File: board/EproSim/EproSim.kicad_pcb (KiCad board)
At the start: 2 copper layers, 85 parts, among them J1 AVR-ISP-6, J2 RS232, J3 Power IN, J4 EXT_ADDR, J5 EXT_D, J6 External Reset, Q1 2N3904, SW1 SW_Push, SW2 Power, U1 ATmega8A-PU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

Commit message: Begin organizing ROsiM board
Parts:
- moved J5 194.8 mm to (114.0, 163.7)
- moved H1 163.7 mm to (95.2, 58.4)
- moved H3 163.3 mm to (95.2, 129.5)
- moved C6 147.9 mm to (97.8, 71.1), turned to 90 degrees
- moved C10 145.1 mm to (113.0, 69.8)
- moved U3 142.1 mm to (123.2, 111.8), turned to 90 degrees
- moved C4 140.7 mm to (105.4, 80.0)
- moved D1 139.4 mm to (95.2, 110.5)
- moved C3 135.9 mm to (128.3, 71.1), turned to 90 degrees
- moved R15 132.9 mm to (110.5, 147.3)
- moved C2 130.6 mm to (94.0, 120.7), turned to 270 degrees
- moved C7 129.3 mm to (119.4, 81.3), turned to 90 degrees
- moved R17 126.8 mm to (184.2, 57.1), turned to 270 degrees
- moved C1 126.7 mm to (94.0, 118.1), turned to 90 degrees
- moved U17 126.2 mm to (171.4, 86.4), turned to 90 degrees
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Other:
- board outline added: 163.8 x 78.7 mm
- board text added: "7-9V TIP positive"
- board text added: "Activity"
- board text added: "CC-BY-SA-4.0"
- board text added: "Power"
- board text added: "Power Switch"
- board text added: "RESET"

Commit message: Begin routing traces
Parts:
- moved J5 168.9 mm to (255.3, 71.1)
- moved R2 148.2 mm to (135.9, 73.7), turned to 90 degrees
- moved R3 147.0 mm to (138.4, 73.7), turned to 90 degrees
- moved C22 144.8 mm to (247.7, 58.4), turned to 270 degrees
- moved C27 137.9 mm to (181.6, 82.5)
- moved C18 134.9 mm to (208.3, 80.0), turned to 270 degrees
- moved C23 115.4 mm to (228.6, 80.0), turned to 270 degrees
- moved C25 115.2 mm to (154.9, 82.5)
- moved C19 114.7 mm to (181.6, 95.2)
- moved Q1 114.4 mm to (233.7, 118.1)
- moved C20 98.4 mm to (181.6, 108.0)
- moved R5 94.1 mm to (128.3, 130.8)
- moved R8 89.4 mm to (151.1, 128.3)
- moved R7 86.6 mm to (139.7, 130.8)
- moved R4 86.6 mm to (128.3, 128.3)
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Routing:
- net GND: track 0.00 -> 186.8 mm
- net VCC: track 0.00 -> 91.1 mm
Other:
- board size 163.8 x 78.7 mm -> 170.2 x 78.7 mm

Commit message: Move around some components
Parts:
- moved D2 19.1 mm to (204.5, 58.4), turned to 0 degrees
- moved R17 17.3 mm to (201.9, 62.2), turned to 0 degrees
- moved D3 8.89 mm to (213.4, 64.8)
- moved SW2 8.89 mm to (219.7, 59.7)
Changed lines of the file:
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@@
   )
   (module Button_Switch_THT:SW_Slide_1P2T_CK_OS102011MS2Q (layer F.Cu)
-    (at 210.82 59.69 180)
+    (at 219.71 59.69 180)
     (descr "CuK miniature slide switch, OS series, SPDT, https://www.ckswitches.com/media/1428/os.pdf")
     (tags "switch SPDT")
-    (fp_text reference SW2 (at 8.89 0 90) (layer F.SilkS)
+    (fp_text reference SW2 (at -5.08 0 90) (layer F.SilkS)
       (effects (font (size 1 1) (thickness 0.15)))
     )
@@
   )
   (module Resistor_THT:R_Axial_DIN0204_L3.6mm_D1.6mm_P7.62mm_Horizontal (layer F.Cu)
-    (at 218.44 57.15 270)
+    (at 201.93 62.23)
     (descr "Resistor, Axial_DIN0204 series, Axial, Horizontal, pin pitch=7.62mm, 0.167W, length*diameter=3.6*1.6mm^2, http://cdn-reichelt.de/documents/datenblatt/B400/1_4W%23YAG.pdf")
     (tags "Resistor Axial_DIN0204 series Axial Horizontal pin pitch 7.62mm 0.167W length 3.6mm diameter 1.6mm")
-    (fp_text reference R17 (at 3.81 0 90) (layer F.SilkS)
-      (effects (font (size 1 1) (thickness 0.15)))
-    )
-    (fp_text value 1.2K (at 3.81 1.92 90) (layer F.Fab)
-      (effects (font (size 1 1) (thickness 0.15)))
-    )
+    (fp_text reference R17 (at 3.81 0) (layer F.SilkS)
+      (effects (font (size 1 1) (thickness 0.15)))
+    )
+    (fp_text value 1.2K (at 3.81 1.92) (layer F.Fab)
+      (effects (font (size 1 1) (thickness 0.15)))
+    )
+    (fp_text user %R (at 3.81 0) (layer F.Fab)
+      (effects (font (size 0.72 0.72) (thickness 0.108)))
+    )
+    (fp_line (start 8.57 -1.05) (end -0.95 -1.05) (layer F.CrtYd) (width 0.05))
+    (fp_line (start 8.57 1.05) (end 8.57 -1.05) (layer F.CrtYd) (width 0.05))
+    (fp_line (start -0.95 1.05) (end 8.57 1.05) (layer F.CrtYd) (width 0.05))
+    (fp_line (start -0.95 -1.05) (end -0.95 1.05) (layer F.CrtYd) (width 0.05))
+    (fp_line (start 6.68 0) (end 5.73 0) (layer F.SilkS) (width 0.12))
+    (fp_line (start 0.94 0) (end 1.89 0) (layer F.SilkS) (width 0.12))
+    (fp_line (start 5.73 -0.92) (end 1.89 -0.92) (layer F.SilkS) (width 0.12))
+    (fp_line (start 5.73 0.92) (end 5.73 -0.92) (layer F.SilkS) (width 0.12))
+    (fp_line (start 1.89 0.92) (end 5.73 0.92) (layer F.SilkS) (width 0.12))
+    (fp_line (start 1.89 -0.92) (end 1.89 0.92) (layer F.SilkS) (width 0.12))
+    (fp_line (start 7.62 0) (end 5.61 0) (layer F.Fab) (width 0.1))
+    (fp_line (start 0 0) (end 2.01 0) (layer F.Fab) (width 0.1))
+    (fp_line (start 5.61 -0.8) (end 2.01 -0.8) (layer F.Fab) (width 0.1))
+    (fp_line (start 5.61 0.8) (end 5.61 -0.8) (layer F.Fab) (width 0.1))
+    (fp_line (start 2.01 0.8) (end 5.61 0.8) (layer F.Fab) (width 0.1))
     (fp_line (start 2.01 -0.8) (end 2.01 0.8) (layer F.Fab) (width 0.1))
-    (fp_line (start 2.01 0.8) (end 5.61 0.8) (layer F.Fab) (width 0.1))
-    (fp_line (start 5.61 0.8) (end 5.61 -0.8) (layer F.Fab) (width 0.1))
-    (fp_line (start 5.61 -0.8) (end 2.01 -0.8) (layer F.Fab) (width 0.1))
-    (fp_line (start 0 0) (end 2.01 0) (layer F.Fab) (width 0.1))
-    (fp_line (start 7.62 0) (end 5.61 0) (layer F.Fab) (width 0.1))
-    (fp_line (start 1.89 -0.92) (end 1.89 0.92) (layer F.SilkS) (width 0.12))
-    (fp_line (start 1.89 0.92) (end 5.73 0.92) (layer F.SilkS) (width 0.12))
-    (fp_line (start 5.73 0.92) (end 5.73 -0.92) (layer F.SilkS) (width 0.12))
-    (fp_line (start 5.73 -0.92) (end 1.89 -0.92) (layer F.SilkS) (width 0.12))
-    (fp_line (start 0.94 0) (end 1.89 0) (layer F.SilkS) (width 0.12))
-    (fp_line (start 6.68 0) (end 5.73 0) (layer F.SilkS) (width 0.12))
-    (fp_line (start -0.95 -1.05) (end -0.95 1.05) (layer F.CrtYd) (width 0.05))
-    (fp_line (start -0.95 1.05) (end 8.57 1.05) (layer F.CrtYd) (width 0.05))
-    (fp_line (start 8.57 1.05) (end 8.57 -1.05) (layer F.CrtYd) (width 0.05))
-    (fp_line (start 8.57 -1.05) (end -0.95 -1.05) (layer F.CrtYd) (width 0.05))
-    (fp_text user %R (at 3.81 0 90) (layer F.Fab)
-      (effects (font (size 0.72 0.72) (thickness 0.108)))
-    )
-    (pad 2 thru_hole oval (at 7.62 0 270) (size 1.4 1.4) (drill 0.7) (layers *.Cu *.Mask)
-      (net 2 GND))
-    (pad 1 thru_hole circle (at 0 0 270) (size 1.4 1.4) (drill 0.7) (layers *.Cu *.Mask)
+    (pad 1 thru_hole circle (at 0 0) (size 1.4 1.4) (drill 0.7) (layers *.Cu *.Mask)
       (net 16 "Net-(D2-Pad1)"))
+    (pad 2 thru_hole oval (at 7.62 0) (size 1.4 1.4) (drill 0.7) (layers *.Cu *.Mask)
+      (net 2 GND))
     (model ${KISYS3DMOD}/Resistor_THT.3dshapes/R_Axial_DIN0204_L3.6mm_D1.6mm_P7.62mm_Horizontal.wrl
       (at (xyz 0 0 0))
@@
   )
   (module Diode_THT:D_DO-41_SOD81_P10.16mm_Horizontal (layer F.Cu)
-    (at 204.47 64.77)
+    (at 213.36 64.77)
     (descr "Diode, DO-41_SOD81 series, Axial, Horizontal, pin pitch=10.16mm, , length*diameter=5.2*2.7mm^2, , http://www.diodes.com/_files/packages/DO-41%20(Plastic).pdf")
     (tags "Diode DO-41_SOD81 series Axial Horizontal pin pitch 10.16mm  length 5.2mm diameter 2.7mm")
@@
   )
   (module LED_THT:LED_D2.0mm_W4.8mm_H2.5mm_FlatTop (layer F.Cu)
-    (at 223.52 57.15 270)
+    (at 204.47 58.42)
     (descr "LED, Round, FlatTop,  Rectangular size 4.8x2.5mm^2 diameter 2.0mm, 2 pins, http://www.kingbright.com/attachments/file/psearch/000/00/00/L-13GD(Ver.11B).pdf")
     (tags "LED Round FlatTop  Rectangular size 4.8x2.5mm^2 diameter 2.0mm 2 pins")
-    (fp_text reference D2 (at 1.27 -2.54 90) (layer F.SilkS)
-      (effects (font (size 1 1) (thickness 0.15)))
-    )
-    (fp_text value POWER_LED (at 1.27 2.31 90) (layer F.Fab)
-      (effects (font (size 1 1) (thickness 0.15)))
-    )
+    (fp_text reference D2 (at 1.27 -2.54) (layer F.SilkS)
+      (effects (font (size 1 1) (thickness 0.15)))
+    )
+    (fp_text value POWER_LED (at 1.27 2.31) (layer F.Fab)
+      (effects (font (size 1 1) (thickness 0.15)))
+    )
+    (fp_line (start 4 -1.6) (end -1.45 -1.6) (layer F.CrtYd) (width 0.05))
+    (fp_line (start 4 1.6) (end 4 -1.6) (layer F.CrtYd) (width 0.05))
+    (fp_line (start -1.45 1.6) (end 4 1.6) (layer F.CrtYd) (width 0.05))
+    (fp_line (start -1.45 -1.6) (end -1.45 1.6) (layer F.CrtYd) (width 0.05))
+    (fp_line (start -0.95 1.08) (end -0.95 1.31) (layer F.SilkS) (width 0.12))
+    (fp_line (start -0.95 -1.31) (end -0.95 -1.08) (layer F.SilkS) (width 0.12))
+    (fp_line (start -1.07 1.08) (end -1.07 1.31) (layer F.SilkS) (width 0.12))
+    (fp_line (start -1.07 -1.31) (end -1.07 -1.08) (layer F.SilkS) (width 0.12))
+    (fp_line (start 3.73 -1.31) (end 3.73 1.31) (layer F.SilkS) (width 0.12))
+    (fp_line (start -1.19 -1.31) (end -1.19 1.31) (layer F.SilkS) (width 0.12))
+    (fp_line (start -1.19 1.31) (end 3.73 1.31) (layer F.SilkS) (width 0.12))
+    (fp_line (start -1.19 -1.31) (end 3.73 -1.31) (layer F.SilkS) (width 0.12))
+    (fp_line (start 3.67 -1.25) (end -1.13 -1.25) (layer F.Fab) (width 0.1))
+    (fp_line (start 3.67 1.25) (end 3.67 -1.25) (layer F.Fab) (width 0.1))
+    (fp_line (start -1.13 1.25) (end 3.67 1.25) (layer F.Fab) (width 0.1))
+    (fp_line (start -1.13 -1.25) (end -1.13 1.25) (layer F.Fab) (width 0.1))
     (fp_circle (center 1.27 0) (end 2.27 0) (layer F.Fab) (width 0.1))
-    (fp_line (start -1.13 -1.25) (end -1.13 1.25) (layer F.Fab) (width 0.1))
-    (fp_line (start -1.13 1.25) (end 3.67 1.25) (layer F.Fab) (width 0.1))
-    (fp_line (start 3.67 1.25) (end 3.67 -1.25) (layer F.Fab) (width 0.1))
-    (fp_line (start 3.67 -1.25) (end -1.13 -1.25) (layer F.Fab) (width 0.1))
-    (fp_line (start -1.19 -1.31) (end 3.73 -1.31) (layer F.SilkS) (width 0.12))
-    (fp_line (start -1.19 1.31) (end 3.73 1.31) (layer F.SilkS) (width 0.12))
-    (fp_line (start -1.19 -1.31) (end -1.19 1.31) (layer F.SilkS) (width 0.12))
-    (fp_line (start 3.73 -1.31) (end 3.73 1.31) (layer F.SilkS) (width 0.12))
-    (fp_line (start -1.07 -1.31) (end -1.07 -1.08) (layer F.SilkS) (width 0.12))
-    (fp_line (start -1.07 1.08) (end -1.07 1.31) (layer F.SilkS) (width 0.12))
-    (fp_line (start -0.95 -1.31) (end -0.95 -1.08) (layer F.SilkS) (width 0.12))
-    (fp_line (start -0.95 1.08) (end -0.95 1.31) (layer F.SilkS) (width 0.12))
-    (fp_line (start -1.45 -1.6) (end -1.45 1.6) (layer F.CrtYd) (width 0.05))
-    (fp_line (start -1.45 1.6) (end 4 1.6) (layer F.CrtYd) (width 0.05))
-    (fp_line (start 4 1.6) (end 4 -1.6) (layer F.CrtYd) (width 0.05))
-    (fp_line (start 4 -1.6) (end -1.45 -1.6) (layer F.CrtYd) (width 0.05))
-    (pad 2 thru_hole circle (at 2.54 0 270) (size 1.8 1.8) (drill 0.9) (layers *.Cu *.Mask)
+    (pad 1 thru_hole rect (at 0 0) (size 1.8 1.8) (drill 0.9) (layers *.Cu *.Mask)
+      (net 16 "Net-(D2-Pad1)"))
+    (pad 2 thru_hole circle (at 2.54 0) (size 1.8 1.8) (drill 0.9) (layers *.Cu *.Mask)
       (net 13 /RECT_V12))
-    (pad 1 thru_hole rect (at 0 0 270) (size 1.8 1.8) (drill 0.9) (layers *.Cu *.Mask)
-      (net 16 "Net-(D2-Pad1)"))
     (model ${KISYS3DMOD}/LED_THT.3dshapes/LED_D2.0mm_W4.8mm_H2.5mm_FlatTop.wrl
       (at (xyz 0 0 0))
@@
   (gr_line (start 95.25 133.35) (end 257.81 133.35) (layer Edge.Cuts) (width 0.05))
   (gr_line (start 91.44 58.42) (end 91.44 129.54) (layer Edge.Cuts) (width 0.05))
-  (gr_text Power (at 223.52 63.5) (layer F.SilkS)
+  (gr_text Power (at 205.74 64.77) (layer F.SilkS)
     (effects (font (size 1 1) (thickness 0.15)))
   )
@@
     (effects (font (size 1 1) (thickness 0.15)) (justify mirror))
   )
-  (gr_text "Power Switch" (at 208.28 55.88) (layer F.SilkS)
+  (gr_text "Power Switch" (at 218.44 55.88) (layer F.SilkS)
     (effects (font (size 1 1) (thickness 0.15)))
   )

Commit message: Complete routing
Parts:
- moved R24 119.4 mm to (109.2, 128.3), turned to 0 degrees
- moved Q1 112.1 mm to (121.9, 127.0), turned to 270 degrees
- moved C13 96.3 mm to (227.3, 68.6)
- moved U15 96.3 mm to (221.0, 72.4)
- moved R2 77.5 mm to (213.4, 72.4)
- moved R3 77.5 mm to (215.9, 72.4)
- moved U17 41.9 mm to (213.4, 85.1)
- moved U18 41.9 mm to (213.4, 97.8)
- moved U19 41.9 mm to (213.4, 110.5)
- moved C19 41.9 mm to (223.5, 94.0)
- moved C20 41.9 mm to (223.5, 106.7)
- moved C27 41.9 mm to (223.5, 81.3)
- moved C15 29.2 mm to (167.6, 66.0)
- moved C18 29.2 mm to (179.1, 80.0)
- moved C23 29.2 mm to (199.4, 80.0)
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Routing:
- net GND: track 186.8 -> 879.2 mm
- net VCC: track 91.1 -> 689.6 mm, vias 0 -> 2
- net /SRAM_D2: track 0.00 -> 232.8 mm, vias 0 -> 4
- net /SRAM_A18: track 0.00 -> 226.0 mm, vias 0 -> 2
- net /~EXT_EN: track 0.00 -> 196.8 mm, vias 0 -> 1
- net /SRAM_A5: track 0.00 -> 171.6 mm, vias 0 -> 5
- net /SRAM_A17: track 0.00 -> 160.2 mm, vias 0 -> 2
- net /SRAM_D1: track 0.00 -> 158.3 mm, vias 0 -> 2
- net /SRAM_D3: track 0.00 -> 157.4 mm, vias 0 -> 3
- net /SRAM_A8: track 0.00 -> 156.5 mm, vias 0 -> 3
- net /SRAM_A16: track 0.00 -> 153.8 mm, vias 0 -> 3
- net /~EXT_RESET: track 0.00 -> 147.1 mm
- net /SRAM_D0: track 0.00 -> 146.9 mm, vias 0 -> 3
- net /SRAM_D5: track 0.00 -> 146.1 mm, vias 0 -> 3
- net /SRAM_A11: track 0.00 -> 145.8 mm, vias 0 -> 2
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- added copper zone on B.Cu, net GND
- added copper zone on F.Cu, net GND
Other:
- board text added: "ISP"

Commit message: Update PCB
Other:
- board text added: "External Reset"
- board text added: "ROsiM"
- board text added: "rev.1"
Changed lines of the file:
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@@
   (general
     (thickness 1.6)
-    (drawings 15)
+    (drawings 18)
     (tracks 3238)
     (zones 0)
@@
   (page A4)
   (layers
-    (0 F.Cu signal)
-    (31 B.Cu signal)
+    (0 F.Cu signal hide)
+    (31 B.Cu signal hide)
     (32 B.Adhes user)
     (33 F.Adhes user)
@@
     (descr "Resistor, Axial_DIN0204 series, Axial, Horizontal, pin pitch=7.62mm, 0.167W, length*diameter=3.6*1.6mm^2, http://cdn-reichelt.de/documents/datenblatt/B400/1_4W%23YAG.pdf")
     (tags "Resistor Axial_DIN0204 series Axial Horizontal pin pitch 7.62mm 0.167W length 3.6mm diameter 1.6mm")
-    (fp_text reference R24 (at 3.81 -1.92) (layer F.SilkS)
+    (fp_text reference R24 (at 3.81 0) (layer F.SilkS)
       (effects (font (size 1 1) (thickness 0.15)))
     )
@@
     (descr "Through hole straight socket strip, 1x02, 2.54mm pitch, single row (from Kicad 4.0.7), script generated")
     (tags "Through hole socket strip THT 1x02 2.54mm single row")
-    (fp_text reference J6 (at 0 -2.77) (layer F.SilkS)
+    (fp_text reference J6 (at -3.81 -1.27) (layer F.SilkS)
       (effects (font (size 1 1) (thickness 0.15)))
     )
@@
     (descr "Through hole IDC box header, 2x20, 2.54mm pitch, DIN 41651 / IEC 60603-13, double rows, https://docs.google.com/spreadsheets/d/16SsEcesNF15N3Lb4niX7dcUr-NY5_MFPQhobNuNppn4/edit#gid=0")
     (tags "Through hole vertical IDC box header THT 2x20 2.54mm double row")
-    (fp_text reference J4 (at 1.27 -6.1) (layer F.SilkS)
+    (fp_text reference J4 (at 1.27 -6.35) (layer F.SilkS)
       (effects (font (size 1 1) (thickness 0.15)))
     )
@@
     (descr "DC Barrel Jack")
     (tags "Power Jack")
-    (fp_text reference J3 (at -8.45 5.75 90) (layer F.SilkS)
+    (fp_text reference J3 (at -6.35 -6.35) (layer F.SilkS)
       (effects (font (size 1 1) (thickness 0.15)))
     )
@@
     )
   )
+  (gr_text ROsiM (at 229.87 58.42) (layer F.SilkS)
+    (effects (font (size 2 2) (thickness 0.3) italic))
+  )
+  (gr_text rev.1 (at 229.87 60.96) (layer F.SilkS)
+    (effects (font (size 1.5 1.5) (thickness 0.3)))
+  )
+  (gr_text "External Reset" (at 242.57 130.81) (layer F.SilkS)
+    (effects (font (size 1 1) (thickness 0.25)))
+  )
   (gr_text ISP (at 104.14 96.52 90) (layer F.SilkS)

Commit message: Fix solder mask issue
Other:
- rule pad_to_mask_clearance: 0.051 -> 0

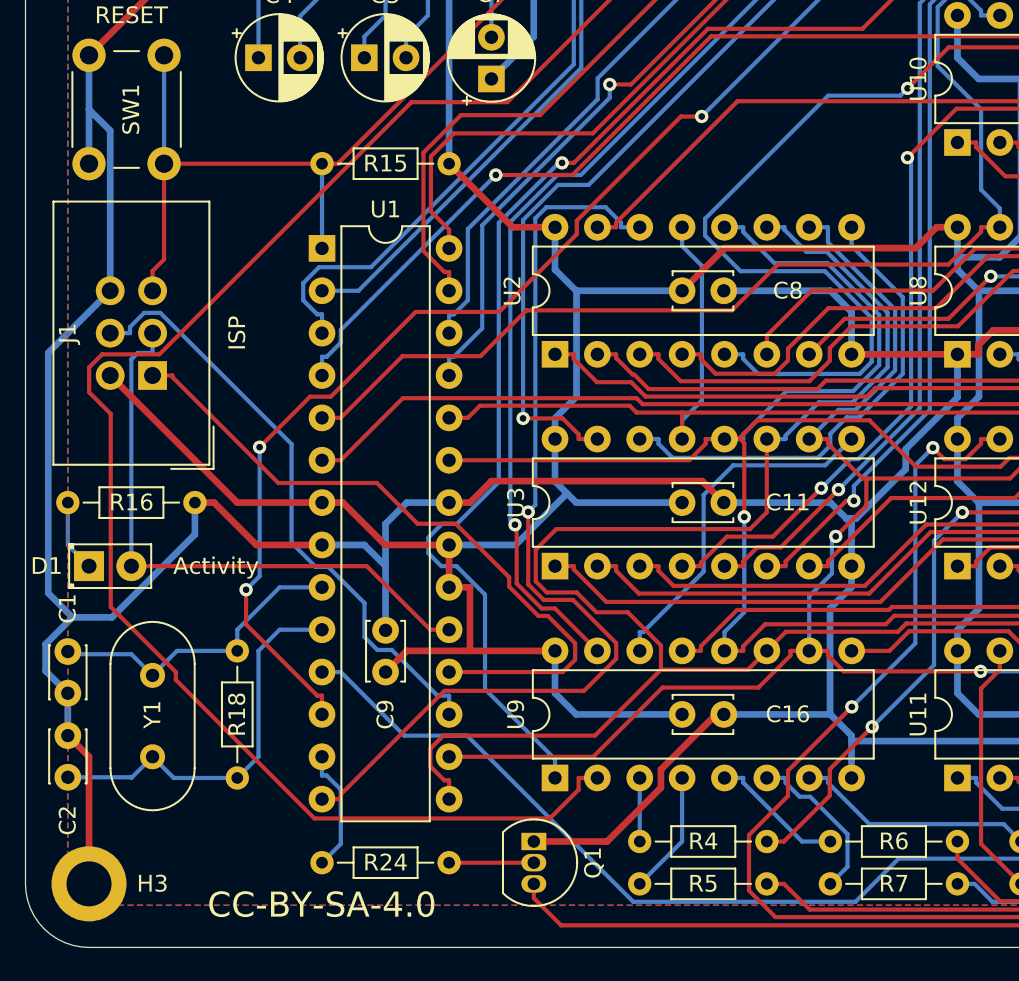
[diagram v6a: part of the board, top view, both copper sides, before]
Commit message: Add resistors to pullup sram selection
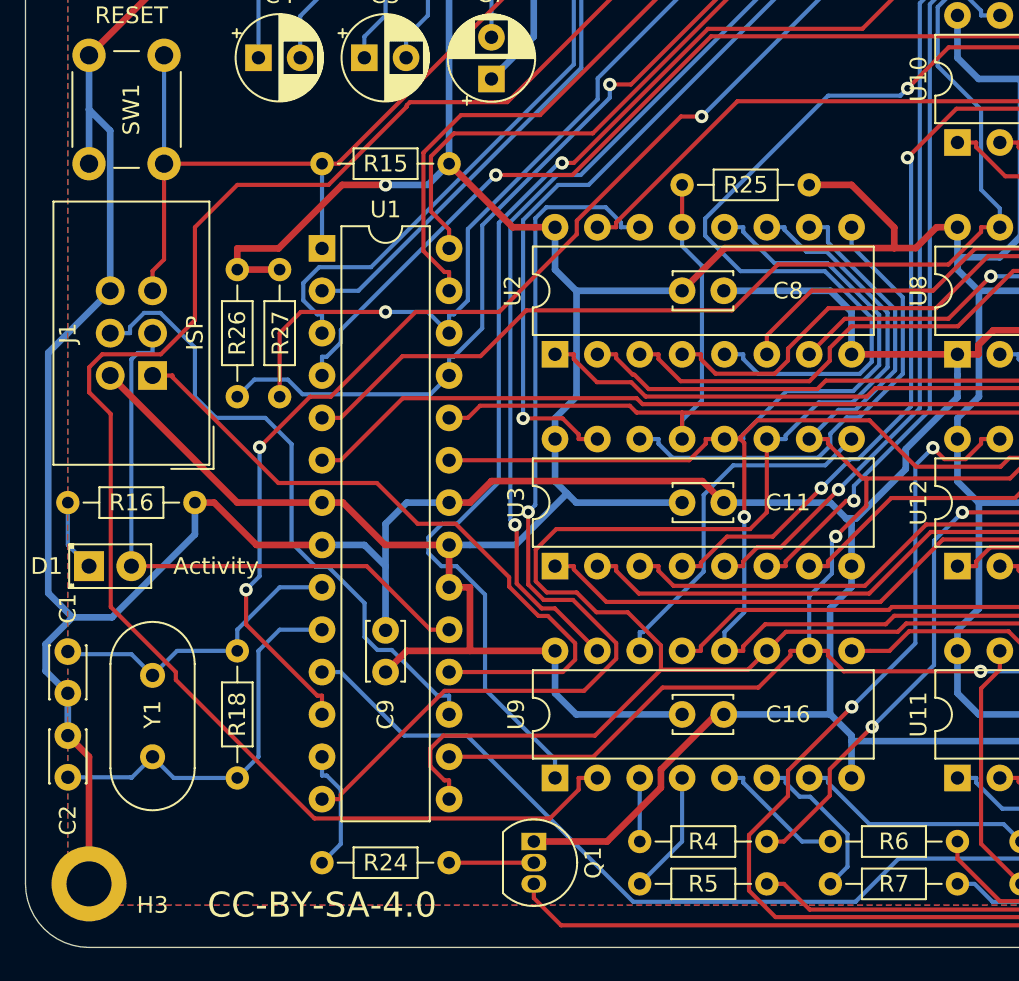
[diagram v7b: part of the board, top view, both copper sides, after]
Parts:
- added R25: 4.7K, Resistor_THT:R_Axial_DIN0204_L3.6mm_D1.6mm_P7.62mm_Horizontal, F.Cu at (130.8, 87.6)
- added R26: 4.7K, Resistor_THT:R_Axial_DIN0204_L3.6mm_D1.6mm_P7.62mm_Horizontal, F.Cu at (104.1, 100.3)
- added R27: 4.7K, Resistor_THT:R_Axial_DIN0204_L3.6mm_D1.6mm_P7.62mm_Horizontal, F.Cu at (106.7, 100.3)
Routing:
- net VCC: track 689.6 -> 715.6 mm, vias 2 -> 3
- net /~SRAM_CE_MCU: track 127.9 -> 142.9 mm, vias 1 -> 2
- net /~EXT_EN: track 196.8 -> 210.7 mm
- net /SRAM_A18: track 226.0 -> 229.3 mm
- net /~SIPO_OE: track 93.7 -> 96.2 mm
- net /MOSI: track 36.3 -> 38.1 mm
